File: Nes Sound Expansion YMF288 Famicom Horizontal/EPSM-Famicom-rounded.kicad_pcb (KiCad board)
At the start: 2 copper layers, 99 x 91.7 mm, 40 parts, among them J1 CARTRIDGE_F, J2 CONSOLE_M, J3 OUT_1, J4 EPSM_ADDRESSING, U1 BU9480F, U10 74LS174, U2 LM321, U3 YMF288, U4 74LS132, U5 74LS139, U6 74LS257, U7 74LS257, U8 74LS257, U9 74LS174, X1 SG-8002CA

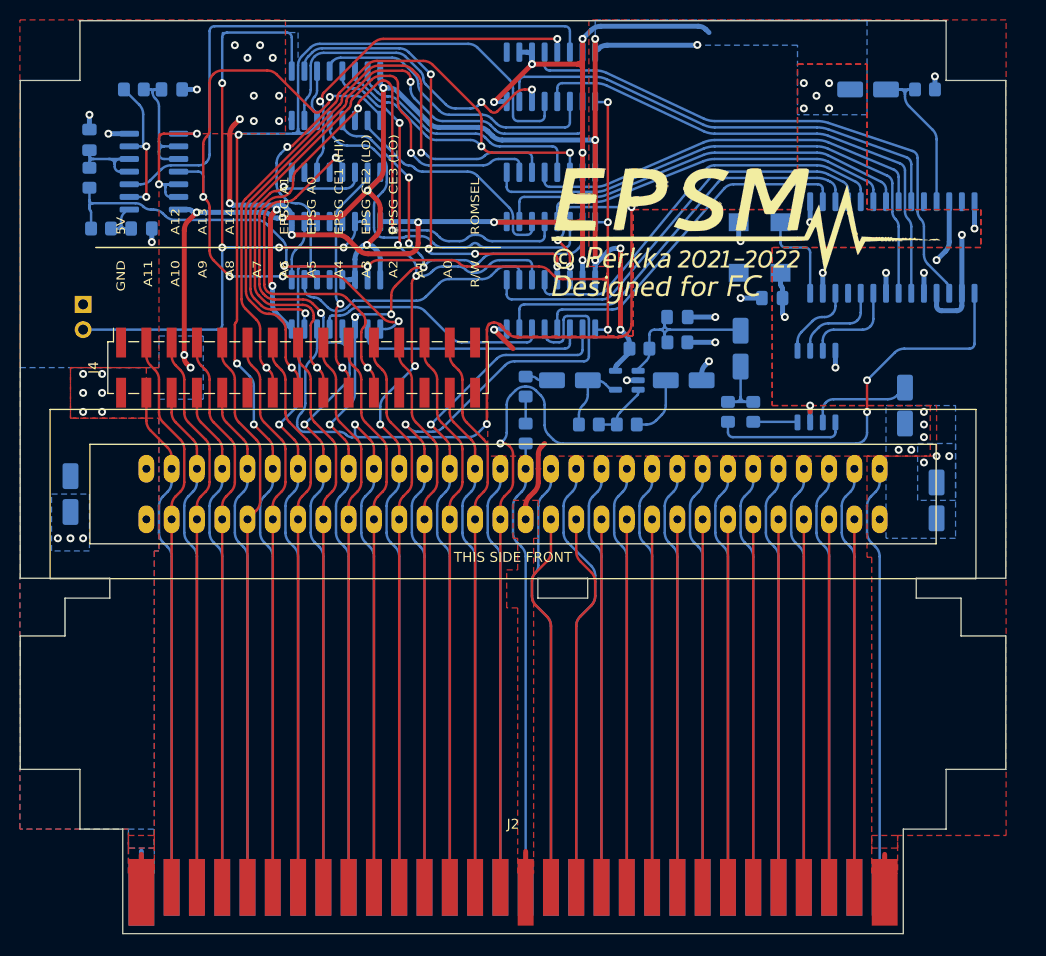
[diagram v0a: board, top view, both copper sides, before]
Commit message: Flip cartridge connection to back instead of front
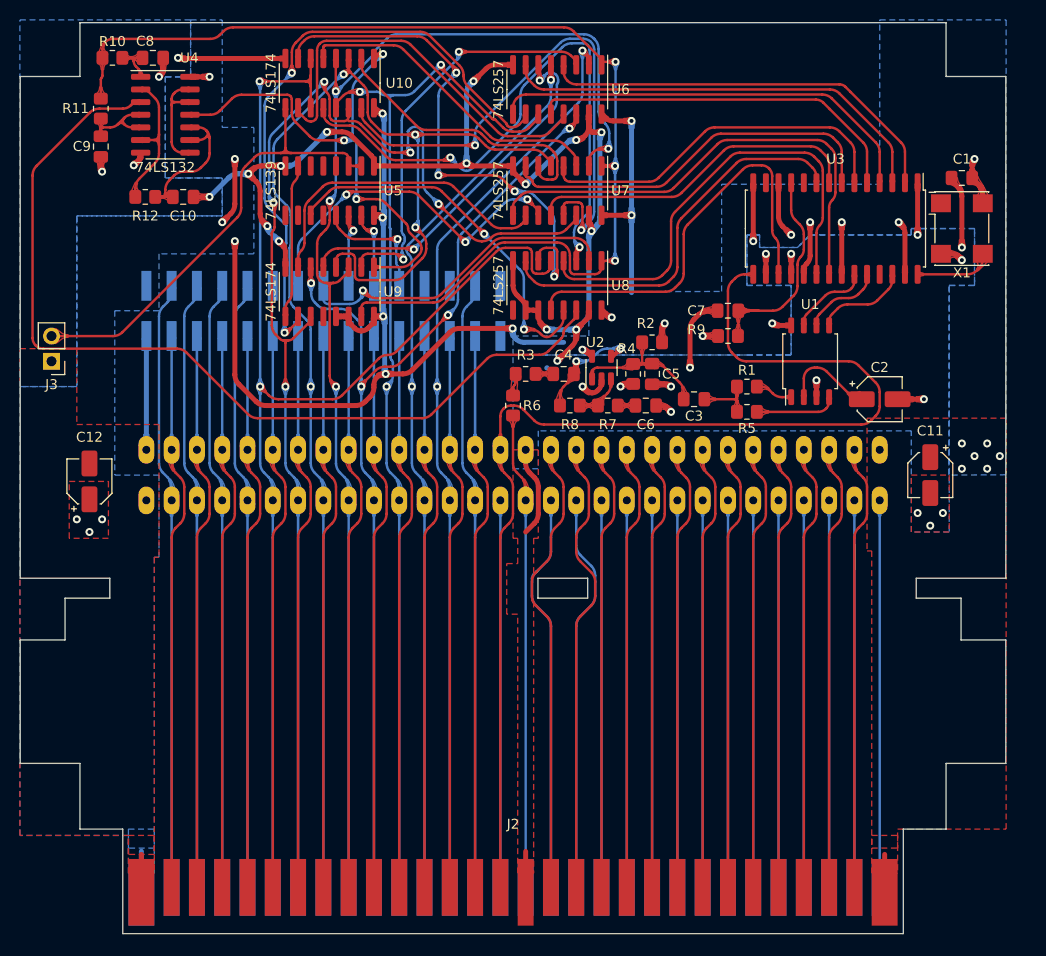
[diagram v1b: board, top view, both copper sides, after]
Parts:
- removed the Ref** at (127.0, 91.4)
- added Ref**: Val**, EPSM-Famicom:Silkscreen-Back, F.Cu at (127.0, 91.8)
- C1, C10, C11, C12, C2, C5, C8, C9, J3, R1, R10, R11, R12, R2, R3, R4, R5, R6, R7, R8, R9, U1, U10, U2, U3, U4, U5, U6, U7, U8, U9, X1: moved to F.Cu
- C3, C4, C6, C7: footprint Capacitor_SMD:CP_Elec_4x5.3 -> Capacitor_SMD:C_0805_2012Metric_Pad1.18x1.45mm_HandSolder; moved to F.Cu
- J1, J4: moved to B.Cu
- moved R9 31.7 mm to (148.6, 77.5), turned to 0 degrees
- moved C7 26.3 mm to (148.6, 74.9)
- moved C1 22.5 mm to (172.1, 61.6)
- moved U6 21.6 mm to (131.4, 52.7), turned to -90 degrees
- moved U8 21.0 mm to (131.4, 72.4), turned to -90 degrees
- moved X1 20.4 mm to (172.1, 66.7), turned to -90 degrees
- moved C8 17.2 mm to (90.8, 49.5)
- moved R10 17.2 mm to (86.8, 49.5)
- moved R12 10.9 mm to (90.1, 63.5)
- moved C10 10.9 mm to (93.9, 63.5)
- moved R11 7.04 mm to (85.6, 54.6), turned to -90 degrees
- moved C3 6.91 mm to (145.2, 83.8), turned to 180 degrees
- moved J3 6.55 mm to (80.6, 80.0)
- moved C5 6.25 mm to (141.0, 81.3), turned to -90 degrees
- moved J4 6.24 mm to (108.0, 75.0), turned to -90 degrees
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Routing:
- net /BUF_D2: track 26.0 -> 62.1 mm, vias 0 -> 2
- net /EPSM_A0_A13: track 67.3 -> 33.4 mm, vias 2 -> 1
- net /BUF_CS: track 60.5 -> 93.3 mm
- net /BUF_D6: track 24.8 -> 55.7 mm, vias 0 -> 2
- net /EPSM_A1_A1: track 65.1 -> 35.2 mm, vias 2 -> 3
- net /CPU_D3: track 131.9 -> 103.2 mm, vias 5 -> 4
- net /BUF_A1: track 30.6 -> 59.2 mm, vias 0 -> 2
- net /EPSM_CE1_A14: track 35.6 -> 7.41 mm, vias 2 -> 1
- net /BUF_A0: track 57.4 -> 31.9 mm, vias 2 -> 0
- net /EPSM_CE3_CPU_R~{W}: track 37.9 -> 12.5 mm, vias 2 -> 1
- net /CPU_D4: track 108.1 -> 131.9 mm, vias 6 -> 4
- net /CPU_D0: track 68.3 -> 92.0 mm, vias 1 -> 2
- net /OUT_1: track 70.2 -> 47.4 mm, vias 4 -> 0
- net /$4016_EN: track 90.6 -> 113.2 mm, vias 5 -> 3
- net /BUF_D7: track 33.8 -> 54.9 mm, vias 2 -> 4
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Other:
- board size 99 x 91.7 mm -> 99 x 91.5 mm
- board text added: "CARTRIDGE FRONT \/"
- board text added: "GND A11 A10 A9 A8 A7 A6 A5 A4 A3 A2 A1 A0 R\W"
- board text added: "VCC M2 A12 A13 A14 EPSG A1 EPSM A0 EPSM CE1 (HI) EPSM CE2 (LO) EPSM CE3 (LO) ROMSEL"
- board text removed: "5V A12 A13 A14 EPSG A1 EPSG A0 EPSG CE1 (HI) EPSG CE2 (LO) EPSG CE3 (LO) ROMSEL"
- board text removed: "GND A11 A10 A9 A8 A7 A6 A5 A4 A3 A2 A1 A0 R/W"

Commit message: Update FC-H EPSM
- Upgrade to 4 layers
- Use same amplifier circuit as NES EPSM
- Optimize logic chip pin assignment
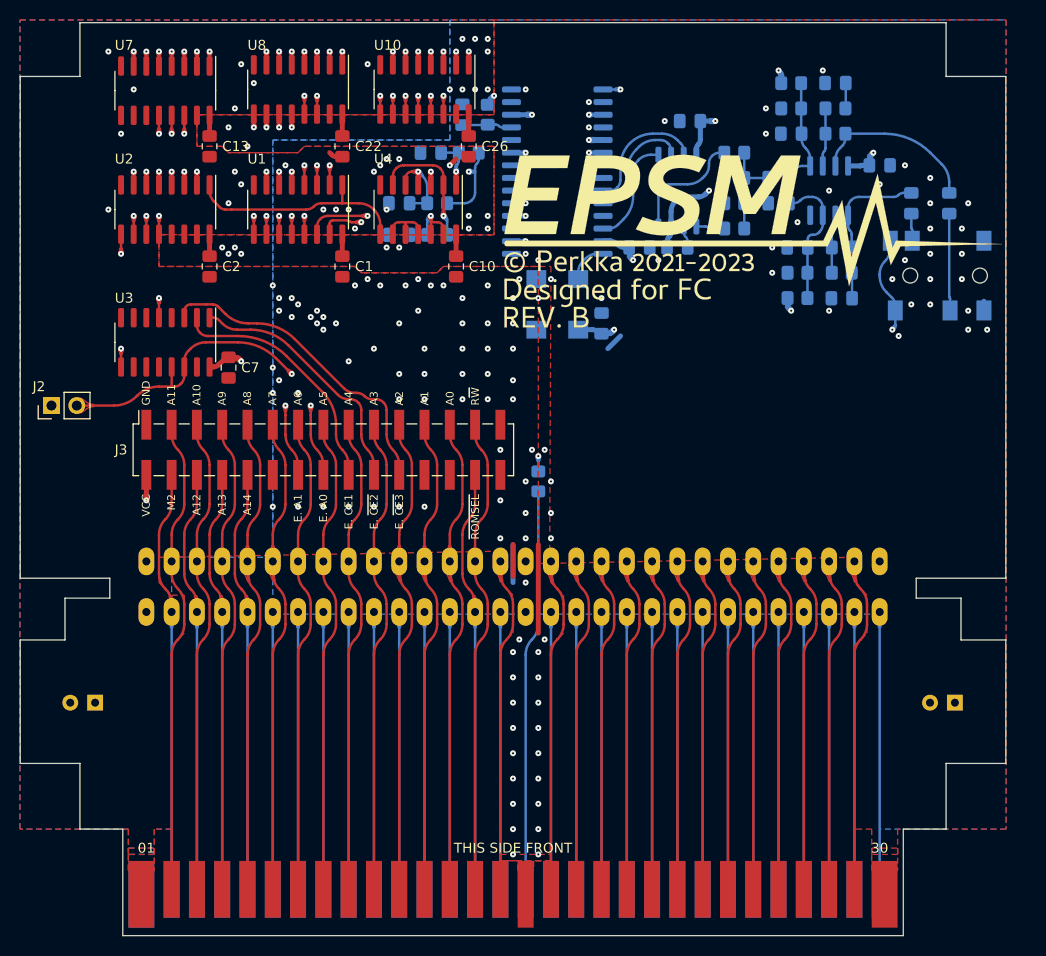
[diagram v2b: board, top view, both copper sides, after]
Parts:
- removed the J4 at (108.0, 75.0)
- removed the Ref** at (127.0, 91.8)
- added C13: 0.1uF, Capacitor_SMD:C_0805_2012Metric_Pad1.18x1.45mm_HandSolder, F.Cu at (96.5, 58.4)
- added C14: 100uF, Capacitor_THT:CP_Radial_D5.0mm_P2.50mm, B.Cu at (85.0, 114.3)
- added C15: 100uF, Capacitor_THT:CP_Radial_D5.0mm_P2.50mm, B.Cu at (171.4, 114.3)
- added C16: 10uF, Capacitor_SMD:C_0805_2012Metric_Pad1.18x1.45mm_HandSolder, B.Cu at (153.7, 64.1)
- added C17: 10uF, Capacitor_SMD:C_0805_2012Metric_Pad1.18x1.45mm_HandSolder, B.Cu at (153.7, 61.6)
- added C18: 68pF, Capacitor_SMD:C_0805_2012Metric_Pad1.18x1.45mm_HandSolder, B.Cu at (155.6, 68.6)
- added C19: 68pF, Capacitor_SMD:C_0805_2012Metric_Pad1.18x1.45mm_HandSolder, B.Cu at (154.9, 57.1)
- added C20: 10uF, Capacitor_SMD:C_0805_2012Metric_Pad1.18x1.45mm_HandSolder, B.Cu at (160.0, 73.7)
- added C21: 10uF, Capacitor_SMD:C_0805_2012Metric_Pad1.18x1.45mm_HandSolder, B.Cu at (159.4, 52.1)
- added C22: 0.1uF, Capacitor_SMD:C_0805_2012Metric_Pad1.18x1.45mm_HandSolder, F.Cu at (109.9, 58.4)
- added C23: 0.1uF, Capacitor_SMD:C_0805_2012Metric_Pad1.18x1.45mm_HandSolder, B.Cu at (163.8, 60.3)
- added C24: 10uF, Capacitor_SMD:C_0805_2012Metric_Pad1.18x1.45mm_HandSolder, B.Cu at (167.0, 64.1)
- added C25: 10uF, Capacitor_SMD:C_0805_2012Metric_Pad1.18x1.45mm_HandSolder, B.Cu at (170.8, 64.1)
- added C26: 0.1uF, Capacitor_SMD:C_0805_2012Metric_Pad1.18x1.45mm_HandSolder, F.Cu at (122.6, 58.4)
- added J2: OUT_1, Connector_PinHeader_2.54mm:PinHeader_1x02_P2.54mm_Vertical, F.Cu at (80.6, 84.5)
- added J5: AudioJack4_SwitchTR1, EPSM-Famicom:Jack_3.5mm_PJ311_Horizontal, B.Cu at (176.5, 71.4)
- added R13: 8.2K, Resistor_SMD:R_0805_2012Metric_Pad1.20x1.40mm_HandSolder, B.Cu at (160.0, 71.1)
- added R14: 8.2K, Resistor_SMD:R_0805_2012Metric_Pad1.20x1.40mm_HandSolder, B.Cu at (159.4, 54.6)
- added R15: 22K, Resistor_SMD:R_0805_2012Metric_Pad1.20x1.40mm_HandSolder, B.Cu at (160.0, 68.6)
- added R16: 22K, Resistor_SMD:R_0805_2012Metric_Pad1.20x1.40mm_HandSolder, B.Cu at (159.4, 57.1)
- added R17: 1K, Resistor_SMD:R_0805_2012Metric_Pad1.20x1.40mm_HandSolder, B.Cu at (129.5, 92.1)
- added Ref**: Val**, EPSM-Famicom:EPSM_silkscreen, F.Cu at (151.1, 67.9)
- C1, C10: value 68pF -> 0.1uF
- C11: footprint Capacitor_SMD:CP_Elec_4x5.3 -> Capacitor_SMD:C_0805_2012Metric_Pad1.18x1.45mm_HandSolder; moved to B.Cu
- C12: value 10uF -> 0.1uF; footprint Capacitor_SMD:CP_Elec_4x5.3 -> Capacitor_SMD:C_0805_2012Metric_Pad1.18x1.45mm_HandSolder; moved to B.Cu
- C2: value 10uF -> 0.1uF; footprint Capacitor_SMD:CP_Elec_4x5.3 -> Capacitor_SMD:C_0805_2012Metric_Pad1.18x1.45mm_HandSolder
- C3, C4: value 10uF -> 68pF; moved to B.Cu
- C5, C6, C9, R1, R3, R6, X1: moved to B.Cu
- C7: value 10uF -> 0.1uF
- C8: value 68pF -> 0.1uF; moved to B.Cu
- J3: value OUT_1 -> EPSM_ADDRESSING; footprint Connector_PinHeader_2.54mm:PinHeader_1x02_P2.54mm_Vertical -> Connector_PinSocket_2.54mm:PinSocket_2x15_P2.54mm_Vertical_SMD
- R10, R12, R9: value 1K -> 47K; moved to B.Cu
- R11: value 3K -> 47K; moved to B.Cu
- R2, R8: value 47K -> 3K; moved to B.Cu
- R4: value 47K -> 1K; moved to B.Cu
- R5: value 1K -> 680; moved to B.Cu
- R7: value 4.7K -> 680; moved to B.Cu
- U1: value BU9480F -> 74LS174; footprint Package_SO:SOIC-8_5.275x5.275mm_P1.27mm -> Package_SO:SOIC-16_3.9x9.9mm_P1.27mm
- U10: value 74LS174 -> 74LS257
- U2: value LM321 -> 74LS174; footprint Package_TO_SOT_SMD:SOT-23-5 -> Package_SO:SOIC-16_3.9x9.9mm_P1.27mm
- U3: value YMF288 -> 74LS139; footprint EPSM-Famicom:SOP-28_7.5x12.8mm_P1.27mm -> Package_SO:SOIC-16_3.9x9.9mm_P1.27mm
- U5: value 74LS139 -> YMF288; footprint Package_SO:SOIC-16_3.9x9.9mm_P1.27mm -> EPSM-Famicom:SOP-28_7.5x12.8mm_P1.27mm; moved to B.Cu
- U6: value 74LS257 -> BU9480F; footprint Package_SO:SOIC-16_3.9x9.9mm_P1.27mm -> Package_SO:SOIC-8_5.275x5.275mm_P1.27mm; moved to B.Cu
- U9: value 74LS174 -> LM358; footprint Package_SO:SOIC-16_3.9x9.9mm_P1.27mm -> Package_SO:SOIC-8_3.9x4.9mm_P1.27mm; moved to B.Cu
- moved R10 72.1 mm to (155.6, 71.1), turned to 180 degrees
- moved C12 70.4 mm to (144.8, 55.9), turned to 0 degrees
- moved R11 69.4 mm to (154.9, 52.1), turned to 0 degrees
- moved C2 68.6 mm to (96.5, 70.5), turned to 90 degrees
- moved U3 68.3 mm to (92.1, 78.1)
- moved R12 65.5 mm to (154.9, 54.6), turned to 180 degrees
- moved C1 62.9 mm to (109.9, 70.5), turned to 90 degrees
- moved U1 53.6 mm to (105.4, 64.8), turned to -90 degrees
- moved C9 53.3 mm to (135.9, 76.2), turned to 90 degrees
- moved C8 52.5 mm to (139.7, 68.6), turned to 180 degrees
- moved U9 51.2 mm to (158.8, 62.9), turned to 90 degrees
- moved C7 50.5 mm to (98.4, 80.6), turned to 90 degrees
- moved U2 46.6 mm to (92.1, 64.8), turned to -90 degrees
- moved X1 41.3 mm to (131.4, 74.3), turned to 90 degrees
- moved U7 40.6 mm to (92.1, 52.8)
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- renumbered J2 to J4
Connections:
- C1 pad 1: /VCC -> /GND
- C1 pad 2: /GND -> /VCC
- C10 pad 1: Net-(C10-Pad1) -> /GND
- C10 pad 2: /GND -> /VCC
- C11 pad 1: /VCC -> Net-(C11-Pad1)
- C12 pad 1: /VCC -> /GND
- C12 pad 2: /GND -> /VCC
- C2 pad 1: Net-(C2-Pad1) -> /GND
- C2 pad 2: /GND -> /VCC
- C3 pad 2: Net-(C3-Pad2) -> /GND
- C4 pad 2: Net-(C4-Pad2) -> /GND
- C5 pad 1: Net-(C3-Pad2) -> Net-(C5-Pad1)
- C6 pad 1: Net-(C6-Pad1) -> /GND
- C6 pad 2: /GND -> Net-(C6-Pad2)
- C7 pad 2: Net-(C7-Pad2) -> /VCC
- C8 pad 1: Net-(C8-Pad1) -> /GND
- C8 pad 2: /GND -> /VCC
- C9 pad 1: Net-(C9-Pad1) -> /VCC
- J3 pad 2: /OUT_1 -> /VCC
- J4 pad 46: /AUD_RF -> /AUD_EPSM
- R1 pad 1: Net-(C3-Pad1) -> /$4016_EN
- R1 pad 2: Net-(R1-Pad2) -> Net-(C3-Pad1)
- R10 pad 1: /$4016_EN -> Net-(C16-Pad2)
- R10 pad 2: Net-(C8-Pad1) -> /GND
- R11 pad 1: /$4016_EN -> /VCC
- R11 pad 2: Net-(C9-Pad1) -> Net-(C17-Pad2)
- R12 pad 1: Net-(R12-Pad1) -> Net-(C17-Pad2)
- R12 pad 2: Net-(C10-Pad1) -> /GND
- R2 pad 1: /VCC -> /$4016_EN
- R2 pad 2: Net-(C3-Pad2) -> Net-(C4-Pad1)
- R3 pad 1: Net-(C4-Pad2) -> Net-(R3-Pad1)
- R3 pad 2: /AUD_EPSM -> Net-(C5-Pad1)
- R4 pad 1: Net-(C3-Pad2) -> /VCC
- R4 pad 2: /GND -> Net-(C6-Pad2)
- R5 pad 1: Net-(R5-Pad1) -> Net-(C16-Pad1)
- R5 pad 2: Net-(C3-Pad1) -> Net-(R5-Pad2)
- R6 pad 1: /AUD_EPSM -> Net-(C16-Pad1)
- R7 pad 1: Net-(C6-Pad1) -> Net-(C17-Pad1)
- R8 pad 1: Net-(R7-Pad2) -> Net-(C17-Pad1)
- R8 pad 2: Net-(C4-Pad1) -> /AUD_RF
- R9 pad 2: Net-(C7-Pad2) -> Net-(C16-Pad2)
- U1 pad 1: Net-(R1-Pad2) -> /FF_RESET
- U1 pad 2: Net-(C2-Pad1) -> /BUF_A0
- U1 pad 3: /GND -> /CPU_D3
- U1 pad 4: Net-(R5-Pad1) -> /CPU_D2
- U1 pad 5: Net-(U1-Pad5) -> /BUF_A1
- U1 pad 6: Net-(U1-Pad6) -> /CPU_D7
- U1 pad 7: Net-(U1-Pad7) -> /BUF_D7
- U1 pad 8: /VCC -> /GND
- U10 pad 1: /FF_RESET -> /$4016_EN
- U10 pad 10: /BUF_D3 -> /BUF_D7
- U10 pad 12: /BUF_A1 -> /YM_A1
- U10 pad 13: /CPU_D2 -> /BUF_A0
- U10 pad 14: /CPU_D6 -> /EPSM_A1_A1
- U10 pad 15: /BUF_D6 -> /GND
- U10 pad 2: /BUF_D5 -> /BUF_CS
- U10 pad 3: /CPU_D5 -> /~{CS}
- U10 pad 4: /CPU_D4 -> /YM_CS
- U10 pad 5: /BUF_D4 -> /EPSM_A0_A13
- U10 pad 6: /CPU_D7 -> /BUF_A1
- U10 pad 7: /BUF_D7 -> /YM_A0
- U10 pad 9: /OUT_1 -> /YM_D7
- U2 pad 1: Net-(C3-Pad2) -> /FF_RESET
- U2 pad 2: /GND -> /BUF_D3
- U2 pad 3: Net-(R7-Pad2) -> /CPU_D7
- U2 pad 4: Net-(C4-Pad1) -> /CPU_D6
- U2 pad 5: /VCC -> /BUF_D2
- U3 pad 1: /GND -> /EPSM_CE2_~{ROMSEL}
- U3 pad 11: Net-(C7-Pad2) -> unconnected-(U3-Pad11)
- U3 pad 12: /VCC -> unconnected-(U3-Pad12)
- U3 pad 13: unconnected-(U3-Pad13) -> /OUT_1
- U3 pad 14: /GND -> /OUT_1
- U3 pad 15: /~{IRQ} -> /GND
- U3 pad 16: /GND -> /VCC
- U3 pad 2: /YM_D0 -> /EPSM_CE1_A14
- U3 pad 3: /YM_D1 -> /EPSM_CE3_CPU_R~{W}
- U3 pad 4: /YM_D2 -> unconnected-(U3-Pad4)
- U3 pad 5: /YM_D3 -> /~{CS}
- U3 pad 6: /YM_D4 -> unconnected-(U3-Pad6)
- U3 pad 7: /YM_D5 -> unconnected-(U3-Pad7)
- U3 pad 8: /YM_D6 -> /GND
- U3 pad 9: /YM_D7 -> /~{OUT_1}
- U4 pad 1: Net-(C8-Pad1) -> Net-(C3-Pad1)
- U4 pad 10: Net-(C10-Pad1) -> Net-(U4-Pad10)
- U4 pad 11: /FF_RESET -> Net-(U4-Pad10)
- U4 pad 12: Net-(U4-Pad12) -> Net-(C5-Pad1)
- U4 pad 13: Net-(U4-Pad12) -> Net-(C5-Pad1)
- U4 pad 2: Net-(R12-Pad1) -> Net-(R3-Pad1)
- U4 pad 4: Net-(C9-Pad1) -> Net-(C4-Pad1)
- U4 pad 5: Net-(C9-Pad1) -> Net-(C4-Pad1)
- U4 pad 6: Net-(R12-Pad1) -> Net-(R3-Pad1)
- U4 pad 8: Net-(U4-Pad12) -> /FF_RESET
- U4 pad 9: Net-(C10-Pad1) -> Net-(U4-Pad10)
- U5 pad 11: /~{CS} -> Net-(C6-Pad2)
- U5 pad 12: unconnected-(U5-Pad12) -> /VCC
- U5 pad 13: /EPSM_CE3_CPU_R~{W} -> unconnected-(U5-Pad13)
- U5 pad 14: /EPSM_CE1_A14 -> /GND
- U5 pad 15: /EPSM_CE2_~{ROMSEL} -> /~{IRQ}
- U5 pad 16: /VCC -> /GND
- U5 pad 2: /OUT_1 -> /YM_D0
- U5 pad 3: /OUT_1 -> /YM_D1
- U5 pad 4: unconnected-(U5-Pad4) -> /YM_D2
- U5 pad 5: unconnected-(U5-Pad5) -> /YM_D3
- U5 pad 6: unconnected-(U5-Pad6) -> /YM_D4
- U5 pad 7: /~{OUT_1} -> /YM_D5
- U5 pad 8: /GND -> /YM_D6
- U5 pad 9: unconnected-(U5-Pad9) -> /YM_D7
- U6 pad 1: /$4016_EN -> Net-(R5-Pad2)
- U6 pad 2: /CPU_D0 -> Net-(C11-Pad1)
- U6 pad 3: /BUF_D0 -> /GND
- U6 pad 4: /YM_D0 -> Net-(R7-Pad2)
- U6 pad 5: /CPU_D1 -> Net-(U5-Pad26)
- U6 pad 6: /BUF_D1 -> Net-(U5-Pad24)
- U6 pad 7: /YM_D1 -> Net-(U5-Pad23)
- U6 pad 8: /GND -> /VCC
- U7 pad 10: /BUF_A0 -> /GND
- U7 pad 11: /EPSM_A1_A1 -> /GND
- U7 pad 12: /YM_D6 -> /YM_D0
- U7 pad 13: /BUF_D6 -> /BUF_D0
- U7 pad 14: /CPU_D6 -> /CPU_D0
- U7 pad 2: /CPU_D4 -> /CPU_D2
- U7 pad 3: /BUF_D4 -> /BUF_D2
- U7 pad 4: /YM_D4 -> /YM_D2
- U7 pad 5: /CPU_D5 -> /CPU_D1
- U7 pad 6: /BUF_D5 -> /BUF_D1
- U7 pad 7: /YM_D5 -> /YM_D1
- U7 pad 9: /YM_A1 -> unconnected-(U7-Pad9)
- U8 pad 10: /GND -> /BUF_D3
- U8 pad 11: /GND -> /CPU_D3
- U8 pad 12: /YM_CS -> /YM_D4
- U8 pad 13: /~{CS} -> /BUF_D4
- U8 pad 14: /BUF_CS -> /CPU_D4
- U8 pad 2: /EPSM_A0_A13 -> /CPU_D6
- U8 pad 3: /BUF_A1 -> /BUF_D6
- U8 pad 4: /YM_A0 -> /YM_D6
- U8 pad 5: /CPU_D7 -> /CPU_D5
- U8 pad 6: /BUF_D7 -> /BUF_D5
- U8 pad 7: /YM_D7 -> /YM_D5
- U8 pad 9: unconnected-(U8-Pad9) -> /YM_D3
- U9 pad 1: /FF_RESET -> Net-(C24-Pad1)
- U9 pad 2: /BUF_D0 -> Net-(R13-Pad2)
- U9 pad 3: /CPU_D4 -> Net-(C16-Pad2)
- U9 pad 4: /CPU_D5 -> /GND
- U9 pad 5: /BUF_D1 -> Net-(C17-Pad2)
- U9 pad 6: /CPU_D3 -> Net-(R14-Pad2)
- U9 pad 7: /BUF_A0 -> Net-(C25-Pad1)
- U9 pad 8: /GND -> /VCC
- X1 pad 3: Net-(U3-Pad28) -> Net-(U5-Pad28)
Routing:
- net /GND: track 204.9 -> 66.3 mm, vias 35 -> 137
- net /VCC: track 163.5 -> 45.4 mm, vias 30 -> 17
- net /BUF_CS: track 93.3 -> 15.4 mm, vias 0 -> 2
- net Net-(J5-PadR1N): track 0.00 -> 52.9 mm, vias 0 -> 2
- net /AUD_EPSM: track 2.24 -> 40.3 mm
- net /BUF_A1: track 59.2 -> 24.3 mm, vias 2 -> 3
- net /BUF_D2: track 62.1 -> 27.4 mm, vias 2 -> 3
- net /BUF_D7: track 54.9 -> 22.9 mm, vias 4 -> 3
- net /BUF_D6: track 55.7 -> 24.5 mm
- net /FF_RESET: track 52.4 -> 22.9 mm, vias 3 -> 0
- net /$4016_EN: track 113.2 -> 85.5 mm, vias 3 -> 7
- net /~{IRQ}: track 116.2 -> 89.3 mm, vias 0 -> 1
- net /CPU_D5: track 140.5 -> 113.8 mm, vias 4 -> 5
- net /YM_A1: track 50.5 -> 26.0 mm, vias 0 -> 2
- net /CPU_D7: track 131.4 -> 107.7 mm, vias 2 -> 5
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- added copper zone on In1.Cu, net /GND
- added copper zone on In2.Cu, net /GND
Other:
- board size 99 x 91.5 mm -> 99 x 91.7 mm
- copper layers 2 -> 4
- board text added: "01"
- board text added: "30"
- board text added: "31"
- board text added: "60"
- board text added: "GND A11 A10 A9 A8 A7 A6 A5 A4 A3 A2 A1 A0 R~{W}"
- board text added: "THIS SIDE BACK"
- board text added: "THIS SIDE FRONT"
- board text added: "VCC M2 A12 A13 A14 E. A1 E. A0 E. CE1 E. ~{CE2} E. ~{CE3} ~{ROMSEL}"
- board text removed: "CARTRIDGE FRONT \/"
- board text removed: "GND A11 A10 A9 A8 A7 A6 A5 A4 A3 A2 A1 A0 R\W"
- board text removed: "VCC M2 A12 A13 A14 EPSG A1 EPSM A0 EPSM CE1 (HI) EPSM CE2 (LO) EPSM CE3 (LO) ROMSEL"

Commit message: Reposition all SMD components to be on top
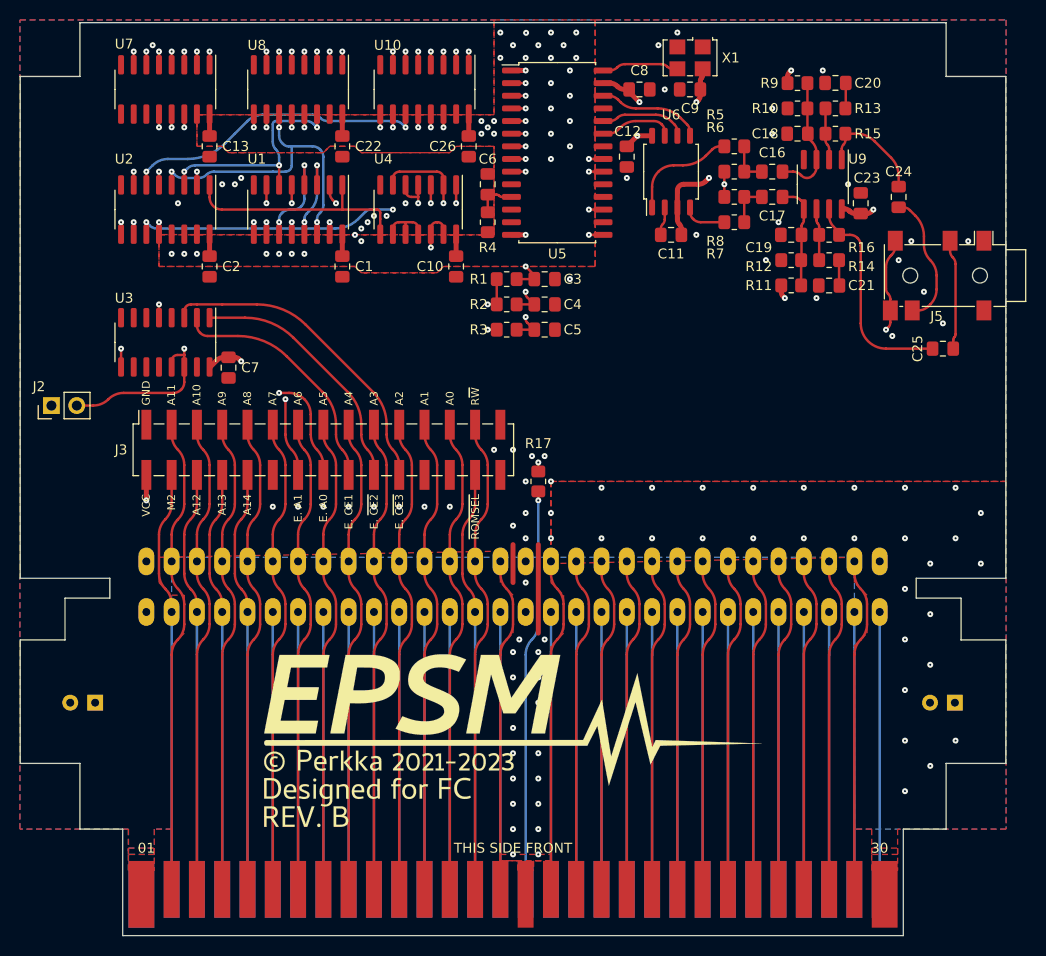
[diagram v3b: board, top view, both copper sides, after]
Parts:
- C11, C12, C16, C17, C18, C19, C20, C21, C23, C24, C25, C3, C4, C5, C6, C8, C9, J5, R1, R10, R11, R12, R13, R14, R15, R16, R17, R2, R3, R4, R5, R6, R7, R8, R9, U5, U6, U9: moved to F.Cu
- X1: footprint Oscillator:Oscillator_SMD_SeikoEpson_SG8002CA-4Pin_7.0x5.0mm -> Oscillator:Oscillator_SMD_SeikoEpson_SG8002LB-4Pin_5.0x3.2mm; moved to F.Cu
- moved Ref** 55.7 mm to (127.0, 118.1)
- moved X1 28.1 mm to (144.8, 49.5), turned to 180 degrees
- moved C9 25.1 mm to (144.8, 52.7), turned to 180 degrees
- moved C20 21.6 mm to (159.4, 52.0)
- moved R9 21.6 mm to (155.6, 52.1)
- moved C21 20.3 mm to (158.8, 72.4)
- moved R11 20.3 mm to (154.9, 72.4)
- moved C4 17.8 mm to (130.2, 74.3), turned to 0 degrees
- moved C5 17.4 mm to (130.2, 76.8), turned to 0 degrees
- moved C3 17.1 mm to (130.2, 71.8), turned to 0 degrees
- moved R13 16.5 mm to (159.4, 54.6)
- moved R10 16.5 mm to (155.6, 54.6)
- moved C8 15.9 mm to (139.7, 52.7)
- moved R14 15.3 mm to (158.8, 69.8)
- moved R12 15.2 mm to (154.9, 69.8)
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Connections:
- U1 pad 14: /CPU_D6 -> /CPU_D7
- U1 pad 15: /BUF_D6 -> /BUF_D3
- U1 pad 2: /BUF_A0 -> /BUF_D0
- U1 pad 3: /CPU_D3 -> /CPU_D4
- U1 pad 4: /CPU_D2 -> /CPU_D5
- U1 pad 5: /BUF_A1 -> /BUF_D1
- U1 pad 6: /CPU_D7 -> /CPU_D6
- U1 pad 7: /BUF_D7 -> /BUF_D2
- U10 pad 10: /BUF_D7 -> /BUF_D3
- U10 pad 11: /CPU_D7 -> /CPU_D3
- U10 pad 12: /YM_A1 -> /YM_D2
- U10 pad 13: /BUF_A0 -> /BUF_D2
- U10 pad 14: /EPSM_A1_A1 -> /CPU_D2
- U10 pad 2: /BUF_CS -> /CPU_D0
- U10 pad 3: /~{CS} -> /BUF_D0
- U10 pad 4: /YM_CS -> /YM_D0
- U10 pad 5: /EPSM_A0_A13 -> /CPU_D1
- U10 pad 6: /BUF_A1 -> /BUF_D1
- U10 pad 7: /YM_A0 -> /YM_D1
- U10 pad 9: /YM_D7 -> /YM_D3
- U2 pad 10: /BUF_D0 -> /BUF_A1
- U2 pad 11: /CPU_D4 -> /CPU_D2
- U2 pad 2: /BUF_D3 -> /BUF_D6
- U2 pad 3: /CPU_D7 -> /CPU_D6
- U2 pad 4: /CPU_D6 -> /CPU_D7
- U2 pad 5: /BUF_D2 -> /BUF_D7
- U2 pad 6: /CPU_D5 -> /CPU_D3
- U2 pad 7: /BUF_D1 -> /BUF_A0
- U7 pad 12: /YM_D0 -> /YM_CS
- U7 pad 13: /BUF_D0 -> /~{CS}
- U7 pad 14: /CPU_D0 -> /BUF_CS
- U7 pad 2: /CPU_D2 -> /EPSM_A1_A1
- U7 pad 3: /BUF_D2 -> /BUF_A0
- U7 pad 4: /YM_D2 -> /YM_A1
- U7 pad 5: /CPU_D1 -> /EPSM_A0_A13
- U7 pad 6: /BUF_D1 -> /BUF_A1
- U7 pad 7: /YM_D1 -> /YM_A0
- U8 pad 10: /BUF_D3 -> /BUF_D7
- U8 pad 11: /CPU_D3 -> /CPU_D7
- U8 pad 12: /YM_D4 -> /YM_D6
- U8 pad 13: /BUF_D4 -> /BUF_D6
- U8 pad 14: /CPU_D4 -> /CPU_D6
- U8 pad 2: /CPU_D6 -> /CPU_D4
- U8 pad 3: /BUF_D6 -> /BUF_D4
- U8 pad 4: /YM_D6 -> /YM_D4
- U8 pad 9: /YM_D3 -> /YM_D7
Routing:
- net /YM_D1: track 52.2 -> 17.6 mm
- net /YM_D2: track 48.0 -> 14.2 mm
- net /YM_D0: track 47.0 -> 13.3 mm
- net /GND: track 66.3 -> 36.5 mm, vias 137 -> 62
- net /~{CS}: track 49.9 -> 20.9 mm, vias 3 -> 2
- net /YM_CS: track 21.5 -> 49.3 mm
- net /YM_A0: track 27.8 -> 54.6 mm
- net /YM_A1: track 26.0 -> 51.8 mm
- net /CPU_D3: track 84.8 -> 109.2 mm, vias 3 -> 2
- net /BUF_CS: track 15.4 -> 36.8 mm, vias 2 -> 3
- net /CPU_D6: track 121.8 -> 102.9 mm, vias 4 -> 3
- net /~{IRQ}: track 89.3 -> 70.8 mm
- net Net-(R3-Pad1): track 13.2 -> 30.5 mm, vias 1 -> 2
- net /YM_D3: track 35.8 -> 18.8 mm
- net /OUT_1: track 48.0 -> 33.7 mm
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- removed copper zone on B.Cu, net /GND
